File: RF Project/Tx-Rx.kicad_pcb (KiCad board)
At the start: 2 copper layers, 30 x 55 mm, 36 parts, among them J1 CONN_Right, J2 CONN_Left, U1 CC2500RGPR, U11 Venus634SMD, U2 U.FL_male, U3 U.FL_male

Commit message: edit vias
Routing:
- net PWR_GND: track 316.8 -> 340.2 mm, vias 141 -> 134
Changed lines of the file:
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@@
   (general
     (links 106)
-    (no_connects 36)
-    (area 84.924999 72.424999 115.075001 127.575001)
+    (no_connects 12)
+    (area 60.150001 62.3 133.85 132.700001)
     (thickness 1.6)
     (drawings 27)
-    (tracks 650)
+    (tracks 657)
     (zones 0)
     (modules 36)
@@
   (segment (start 103 107.28) (end 103 107.425002) (width 0.25) (layer F.Cu) (net 7) (status 30))
   (segment (start 102.5 107.28) (end 103 107.28) (width 0.25) (layer F.Cu) (net 7) (status 30))
-  (via (at 93.99 90.45) (size 0.6) (drill 0.4) (layers F.Cu B.Cu) (net 8))
-  (via (at 92.12 89.38) (size 0.6) (drill 0.4) (layers F.Cu B.Cu) (net 8))
-  (via (at 99.76 79.3) (size 0.6) (drill 0.4) (layers F.Cu B.Cu) (net 8))
-  (via (at 101.33 79.3) (size 0.6) (drill 0.4) (layers F.Cu B.Cu) (net 8))
-  (via (at 101.76 83.51) (size 0.6) (drill 0.4) (layers F.Cu B.Cu) (net 8))
-  (via (at 100.19 83.51) (size 0.6) (drill 0.4) (layers F.Cu B.Cu) (net 8))
-  (via (at 98.67 83.51) (size 0.6) (drill 0.4) (layers F.Cu B.Cu) (net 8))
-  (via (at 97.21 83.51) (size 0.6) (drill 0.4) (layers F.Cu B.Cu) (net 8))
-  (via (at 101.88 89.01) (size 0.6) (drill 0.4) (layers F.Cu B.Cu) (net 8))
-  (via (at 100.31 89.01) (size 0.6) (drill 0.4) (layers F.Cu B.Cu) (net 8))
-  (via (at 98.79 89.01) (size 0.6) (drill 0.4) (layers F.Cu B.Cu) (net 8))
-  (via (at 92.51 82.59) (size 0.6) (drill 0.4) (layers F.Cu B.Cu) (net 8))
-  (via (at 97.33 89.01) (size 0.6) (drill 0.4) (layers F.Cu B.Cu) (net 8))
+  (segment (start 101.3 90.565) (end 101.3 89.39) (width 0.25) (layer F.Cu) (net 8))
+  (segment (start 97.3 90.565) (end 97.3 89.37) (width 0.25) (layer F.Cu) (net 8))
+  (segment (start 97.3 89.37) (end 97.29 89.36) (width 0.25) (layer F.Cu) (net 8))
+  (segment (start 101.3 79.37) (end 101.3 89.39) (width 0.25) (layer B.Cu) (net 8))
+  (segment (start 101.3 90.38) (end 101.3 89.39) (width 0.25) (layer B.Cu) (net 8))
+  (via (at 101.3 89.39) (size 0.6) (drill 0.4) (layers F.Cu B.Cu) (net 8))
+  (segment (start 101.3 80.765) (end 101.3 79.37) (width 0.25) (layer F.Cu) (net 8))
+  (via (at 101.3 79.37) (size 0.6) (drill 0.4) (layers F.Cu B.Cu) (net 8))
+  (via (at 97.29 89.36) (size 0.6) (drill 0.4) (layers F.Cu B.Cu) (net 8))
+  (segment (start 98.1 90.565) (end 98.1 89.36) (width 0.25) (layer F.Cu) (net 8))
+  (via (at 98.1 89.36) (size 0.6) (drill 0.4) (layers F.Cu B.Cu) (net 8))
+  (segment (start 97.04 89.4) (end 97.42 89.02) (width 0.25) (layer B.Cu) (net 8))
+  (segment (start 92.55 89.4) (end 97.04 89.4) (width 0.25) (layer B.Cu) (net 8))
+  (segment (start 92.17 89.02) (end 92.55 89.4) (width 0.25) (layer B.Cu) (net 8))
+  (segment (start 91.41 88.82) (end 91.97 88.82) (width 0.25) (layer F.Cu) (net 8))
+  (segment (start 91.97 88.82) (end 92.17 89.02) (width 0.25) (layer F.Cu) (net 8))
+  (via (at 92.17 89.02) (size 0.6) (drill 0.4) (layers F.Cu B.Cu) (net 8))
+  (segment (start 93.36 82.8) (end 92.84 82.8) (width 0.25) (layer F.Cu) (net 8))
+  (segment (start 92.84 82.8) (end 92.54 82.5) (width 0.25) (layer F.Cu) (net 8))
+  (via (at 92.54 82.5) (size 0.6) (drill 0.4) (layers F.Cu B.Cu) (net 8))
   (segment (start 98 105.7) (end 98 105.285134) (width 0.4) (layer F.Cu) (net 8))
   (segment (start 98 105.285134) (end 97.639246 104.92438) (width 0.4) (layer F.Cu) (net 8))

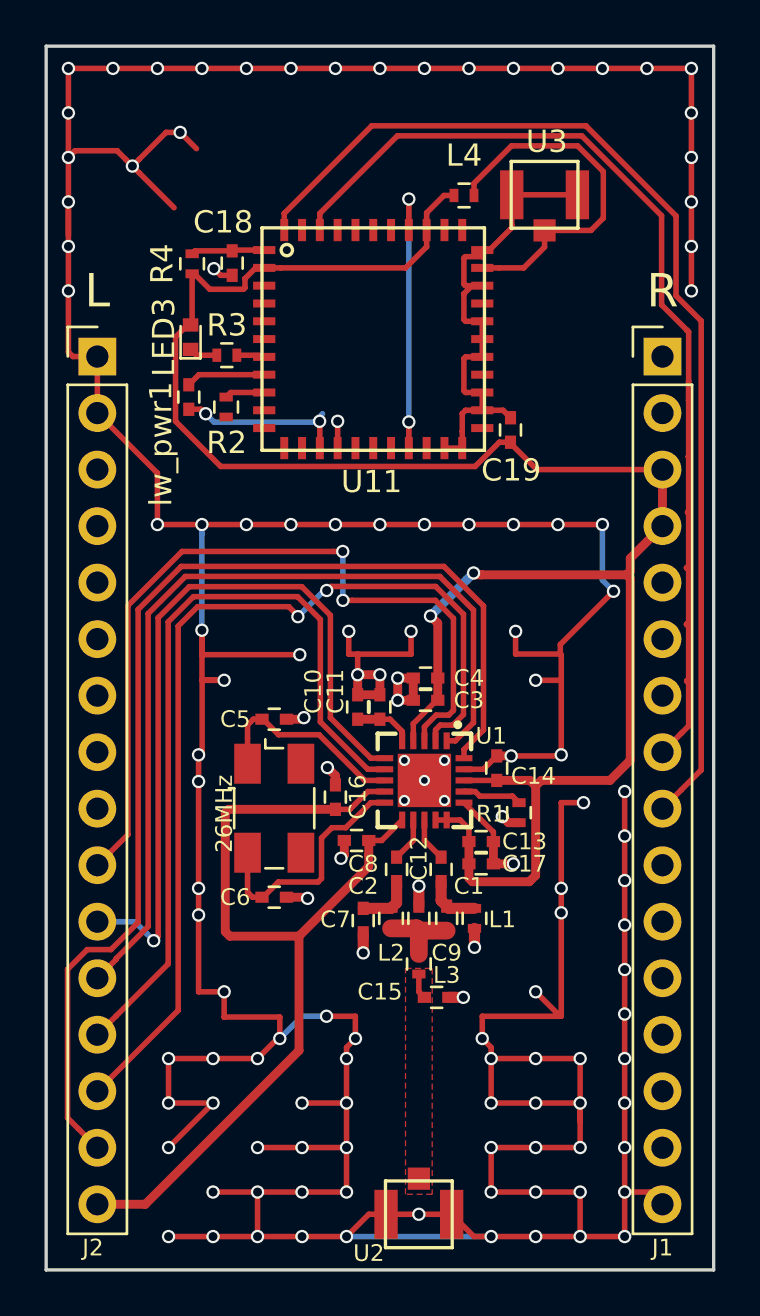
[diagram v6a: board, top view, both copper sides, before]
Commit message: revision component placement, coupling caps added
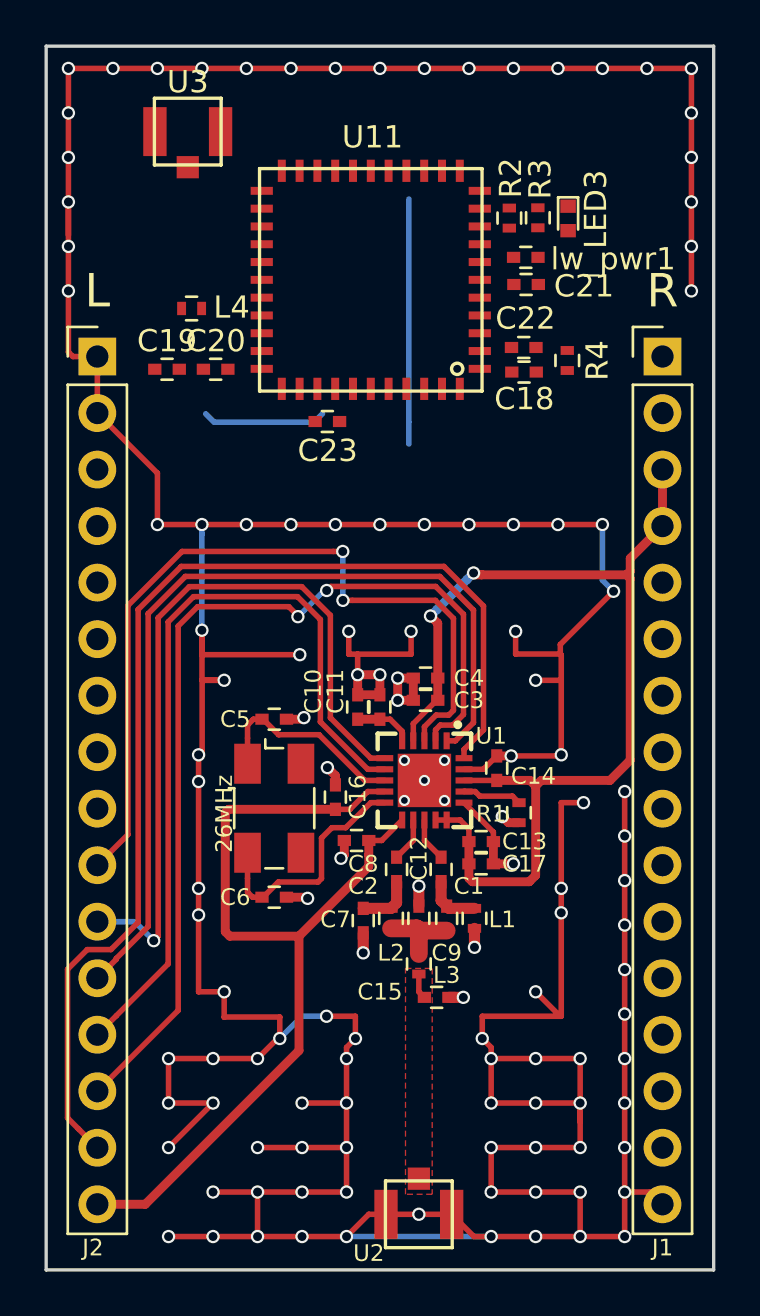
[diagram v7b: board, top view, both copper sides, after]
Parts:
- added C20: 1uF, Capacitors_SMD:C_0402, F.Cu at (92.6, 87.0)
- added C21: 1uF, Capacitors_SMD:C_0402, F.Cu at (106.6, 83.2)
- added C22: 1uF, Capacitors_SMD:C_0402, F.Cu at (106.5, 86.0)
- added C23: 1uF, Capacitors_SMD:C_0402, F.Cu at (97.6, 89.4)
- moved LED3 17.8 mm to (108.5, 80.2), turned to 270 degrees
- moved R4 17.4 mm to (108.4, 86.6), turned to 270 degrees
- moved lw_pwr1 16.4 mm to (106.6, 82.0), turned to 0 degrees
- moved U3 16.3 mm to (91.4, 76.3)
- moved C19 15.7 mm to (90.4, 87.0), turned to 0 degrees
- moved R2 15.3 mm to (105.8, 80.2), turned to 90 degrees
- moved R3 15.3 mm to (107.1, 80.2), turned to 270 degrees
- moved C18 14.0 mm to (106.5, 87.1), turned to 0 degrees
- moved L4 13.3 mm to (91.5, 84.3)
- moved U11 11.1 mm to (104.5, 87.0), turned to 180 degrees
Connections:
- C19 pad 1: RF_GND -> PWR_GND
- L4 pad 2: /GPS/RFIN -> AVDD
- R3 pad 2: NAV -> AVDD
- U11 pad 21: RF_GND -> PWR_GND
- U11 pad 22: RF_GND -> PWR_GND
- U11 pad 24: RF_GND -> PWR_GND
- U11 pad 25: RF_GND -> PWR_GND
- U11 pad 27: RF_GND -> PWR_GND
- U11 pad 28: RF_GND -> PWR_GND
- U11 pad 29: RF_GND -> PWR_GND
- U11 pad 31: RF_GND -> PWR_GND
- U11 pad 32: /GPS/RFIN -> AVDD
- U11 pad 33: RF_GND -> PWR_GND
- U11 pad 7: NAV -> AVDD
- U3 pad 1: RF_GND -> PWR_GND
- U3 pad 2: RF_GND -> PWR_GND
- U3 pad 3: /GPS/RFIN -> AVDD
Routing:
- net TX: track 49.5 -> 0.00 mm
- net AVDD: track 136.1 -> 90.4 mm
- net RX: track 44.5 -> 0.00 mm
- net PWR_GND: track 340.2 -> 307.1 mm, vias 134 -> 126
- net RF_GND: track 22.6 -> 0.00 mm
- net (no net): track 0.00 -> 16.6 mm
- net /GPS/RFIN: track 16.4 -> 0.00 mm
- net GPIO24: track 3.58 -> 0.00 mm
- net /GPS/RSTN: track 3.31 -> 0.00 mm
- net /GPS/BTSEL: track 1.79 -> 0.00 mm
- net Net-(LED3-Pad1): track 1.29 -> 0.00 mm
- net NAV: track 1.26 -> 0.00 mm
